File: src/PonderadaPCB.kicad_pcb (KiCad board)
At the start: 2 copper layers, 7 parts, among them Q1 BC337, SW1 SW_SPDT, U1 Pico

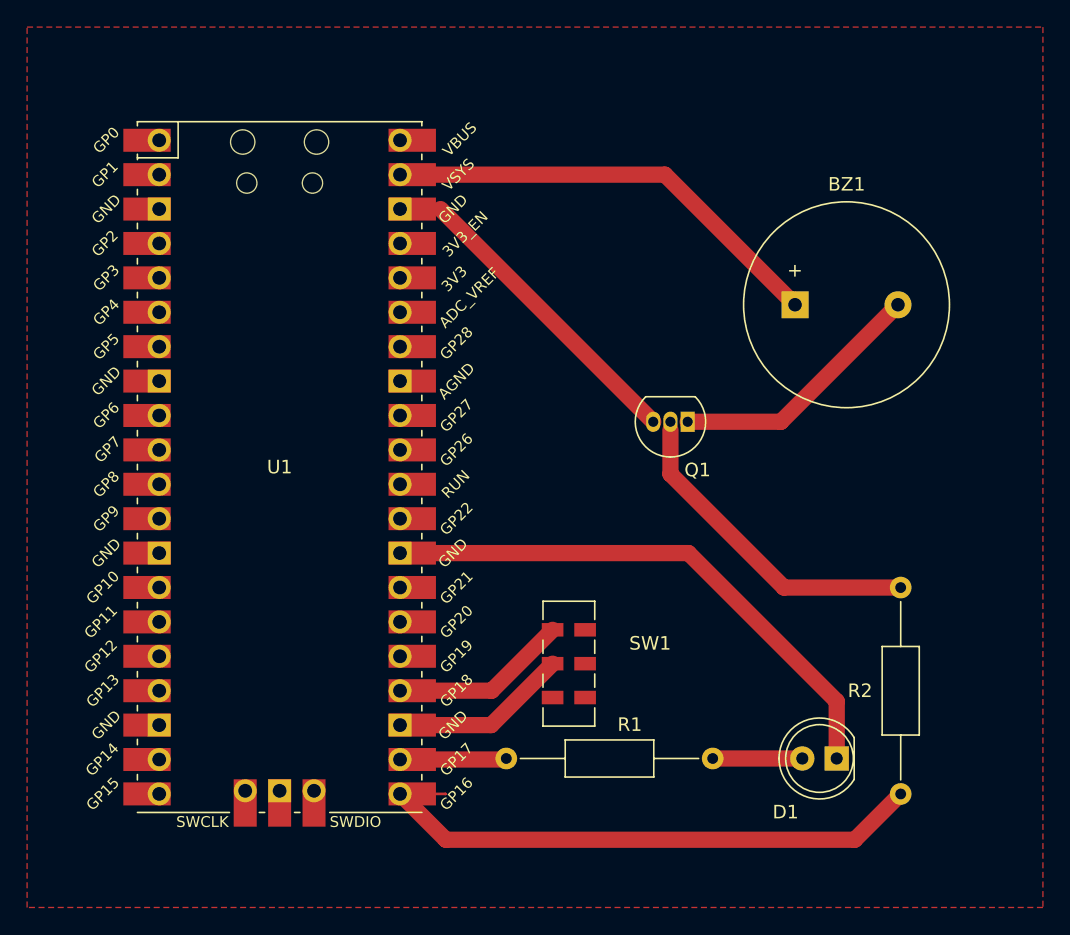
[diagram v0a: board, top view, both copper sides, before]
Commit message: Mudar modelo do Switch
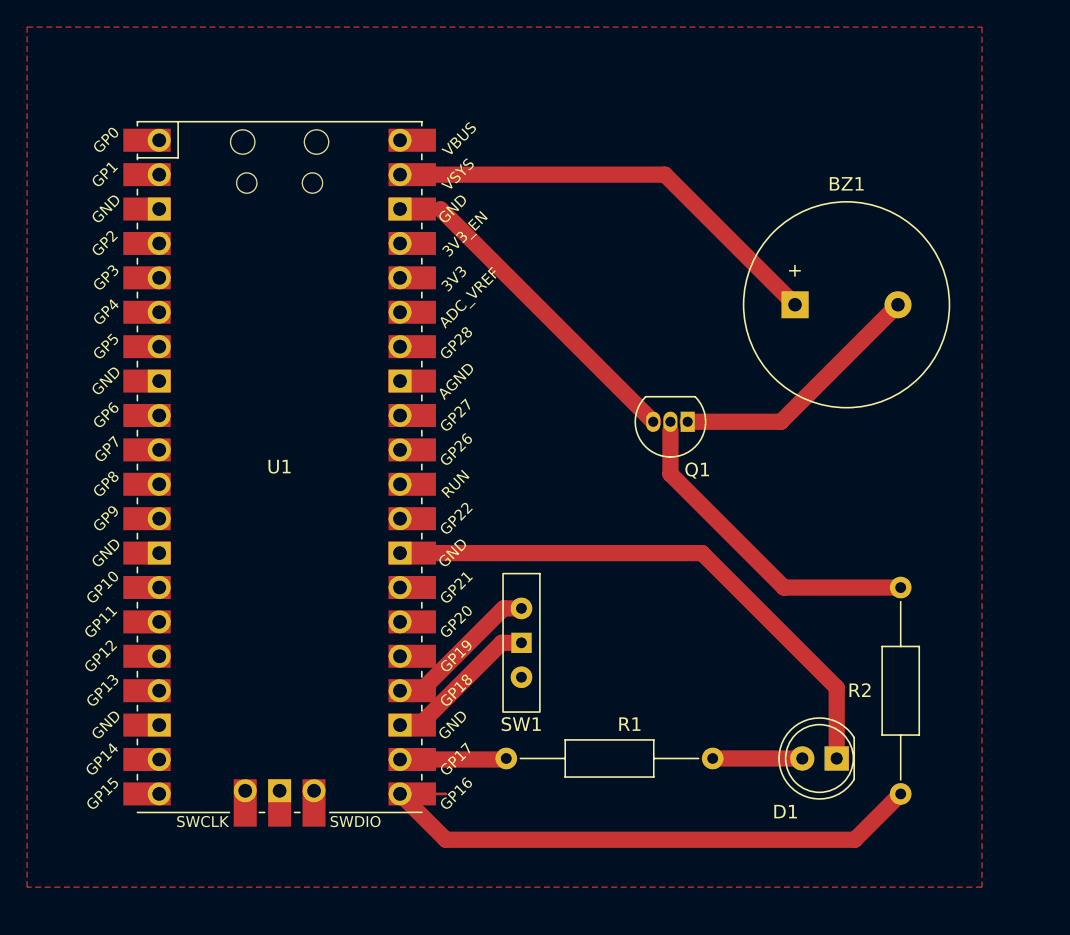
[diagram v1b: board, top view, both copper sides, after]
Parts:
- SW1: value SW_SPDT -> SW_Wuerth_450301014042; footprint Button_Switch_SMD:SW_DPDT_CK_JS202011JCQN -> Button_Switch_THT:SW_Slide-03_Wuerth-WS-SLTV_10x2.5x6.4_P2.54mm
- moved SW1 3.82 mm to (161.5, 110.5), turned to -90 degrees
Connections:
- SW1 pad 1: unconnected-(SW1-A-Pad1) -> GND (Switch)
- SW1 pad 3: GP18 (Switch) -> unconnected-(SW1-A-Pad3)
- U1 pad 24: GP18 (Switch) -> GND (Switch)
- U1 pad 25: unconnected-(U1-GPIO19-Pad25) -> GND (Switch)
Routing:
- net GP18 (Switch): track 13.1 -> 0.00 mm
- net GND (Switch): track 13.1 -> 23.0 mm
- net GND (LED): track 41.2 -> 41.8 mm

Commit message: Consertar circuito de Switch
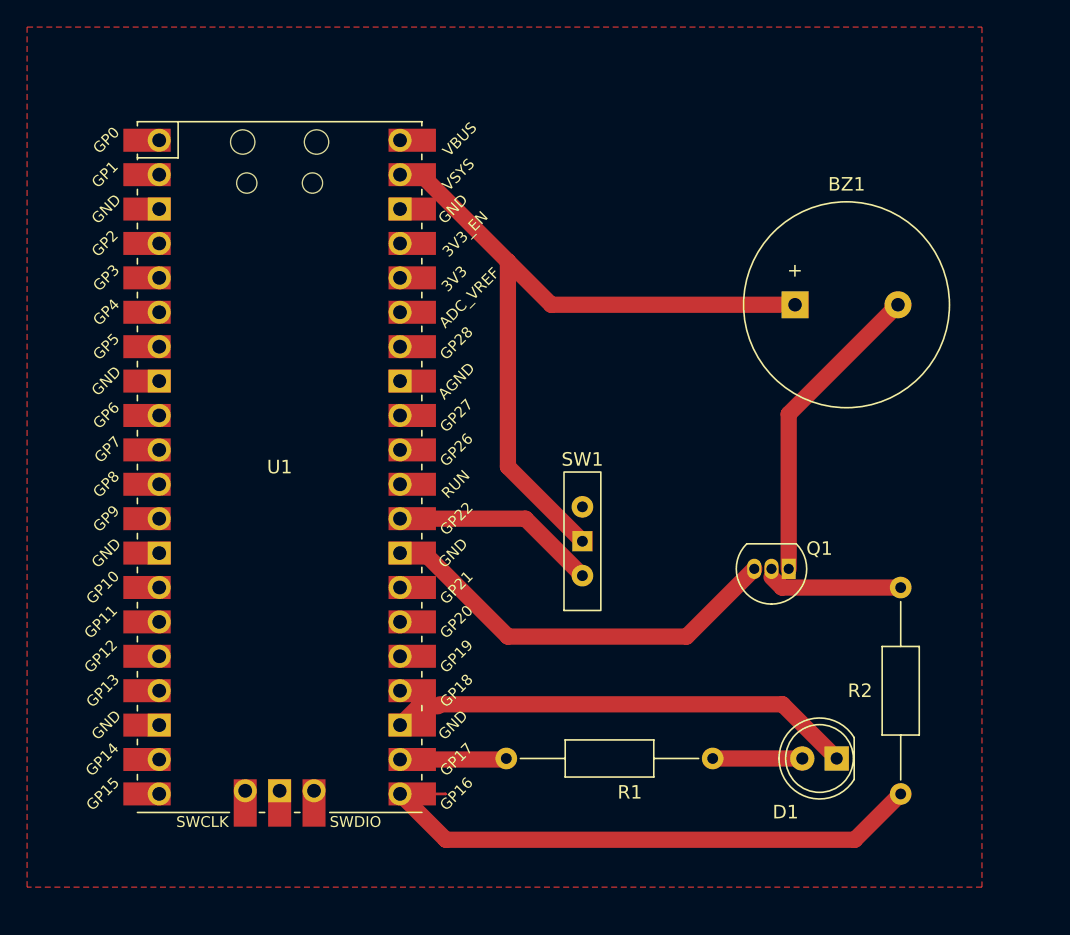
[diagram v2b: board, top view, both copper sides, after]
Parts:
- moved Q1 13.2 mm to (181.2, 105.0)
- moved SW1 8.75 mm to (166.0, 103.0), turned to 90 degrees
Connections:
- BZ1 pad 2: Net-(BZ1--) -> Net-(Q1-B)
- Q1 pad 1: Net-(BZ1--) -> Net-(Q1-B)
- SW1 pad 1: GND (Switch) -> VCC
- SW1 pad 2: GND (Switch) -> GP22 (Switch)
- U1 pad 23: GND (Switch) -> GND (LED)
- U1 pad 24: GND (Switch) -> GND (LED)
- U1 pad 25: GND (Switch) -> unconnected-(U1-GPIO19-Pad25)
- U1 pad 27: unconnected-(U1-GPIO21-Pad27) -> GND (Buzzer)
- U1 pad 28: GND (LED) -> GND (Buzzer)
- U1 pad 29: unconnected-(U1-GPIO22-Pad29) -> GP22 (Switch)
- U1 pad 38: GND (Buzzer) -> VCC
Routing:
- net GND (Switch): track 23.0 -> 0.00 mm
- net VCC: track 34.0 -> 56.9 mm
- net Net-(BZ1--): track 19.1 -> 0.00 mm
- net GP22 (Switch): track 0.00 -> 15.2 mm
- net Net-(Q1-B): track 24.3 -> 33.3 mm
- net GND (LED): track 41.8 -> 34.5 mm
- net GND (Buzzer): track 25.2 -> 31.0 mm
